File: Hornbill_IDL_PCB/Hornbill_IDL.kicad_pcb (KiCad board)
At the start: 2 copper layers, 95.5 x 60 mm, 72 parts, among them CON1 USB-MINI-B, IC1 MCP73831, M1 ESP-WROOM-32, P1 LIPO, P10 CONN_01X10, P11 CONN_01X10, P12 CONN_01X10, P2 CONN_01X02, P3 CONN_01X02, P4 CONN_01X10, P5 CONN_01X10, P6 CONN_01X10, P7 CONN_01X10, P8 CONN_01X10, P9 CONN_01X10, Q1 IRLML5203, Q3 S8050, Q4 S8050, SW1 SW_PUSH, SW2 SW_PUSH, U1 SD_Crard, U10 3.5MM_JACK, U11 MAX6675, U12 AP2112K, U13 3.5MM_JACK, U14 MountingHole, U15 MountingHole, U2 OSH_Symbol, U3 EE_Logo, U4 EE_Logo, U5 MountingHole, U6 MountingHole, U7 MountingHole, U8 MountingHole, U9 CP2102, Y1 32.768KHz RTC Crystal

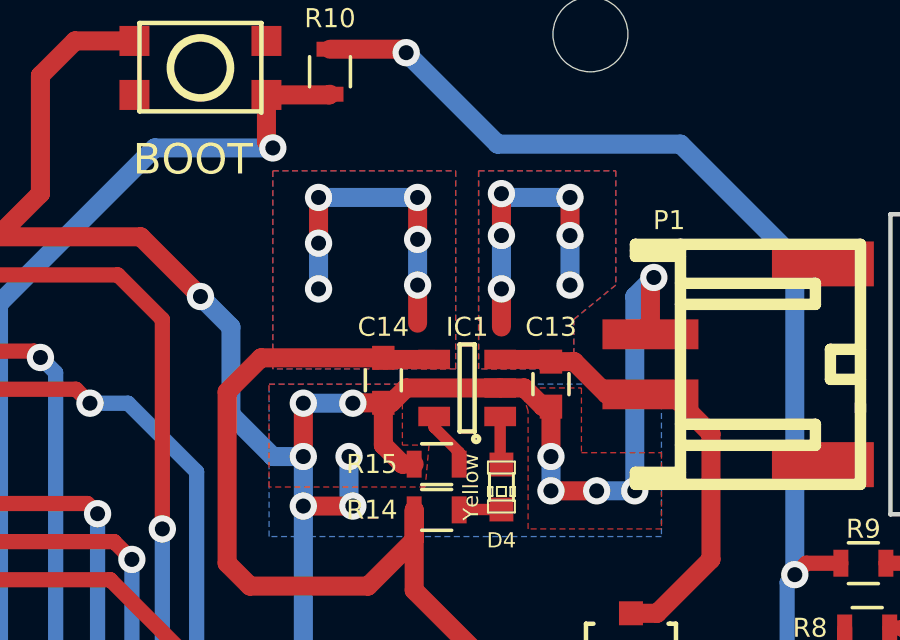
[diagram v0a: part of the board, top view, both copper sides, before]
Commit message: Filled charger zone
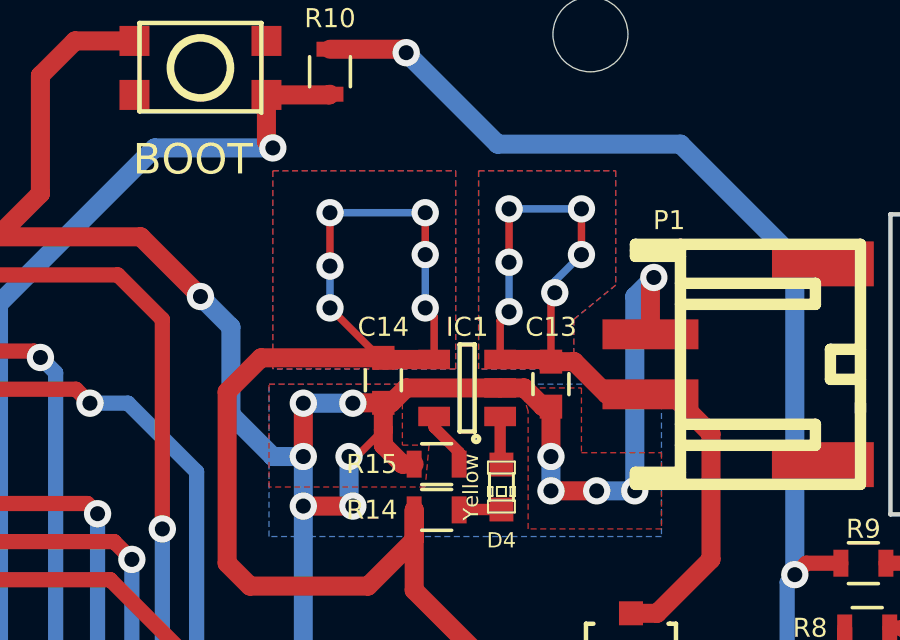
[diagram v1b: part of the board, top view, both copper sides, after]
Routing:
- net (no net): track 20.2 -> 0.00 mm, vias 12 -> 0
- net VCC: track 64.8 -> 78.6 mm, vias 2 -> 8
- net +BATT: track 15.8 -> 28.8 mm, vias 0 -> 6
- net GND: track 364.6 -> 366.1 mm

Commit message: Gerber file generated for v0.1
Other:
- board text added: "v0.1"
